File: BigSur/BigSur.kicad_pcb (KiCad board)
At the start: 2 copper layers, 123.5 x 131.5 mm, 152 parts, among them J1 XT30PW-M, J10 XT30PW-M, J12 XT30PW-M, J14 XT30PW-M, J15 XT30PW-M, J16 XT30PW-M, J2 XT30PW-M, J3 XT30PW-M, J4 XT30PW-M, J5 XT30PW-M, J6 XT30PW-M, J7 XT30PW-M, J8 XT30PW-M, J9 XT30PW-M, K1 G5LE-1A-VDDC12, K2 G5LE-1A-VDDC12, K3 G5LE-1A-VDDC12, K4 G5LE-1A-VDDC12, Q1 TSM900N10, Q2 TSM900N10, Q3 MMBT3904-7-F, Q4 MMBT3904-7-F, Q5 MMBT3904-7-F, Q6 MMBT3904-7-F, U1 DRV103H, U10 MCP6L02T-E_MS, U11 74LVC1G08W5-7, U12 ACS70331EESATR-2P5U3, U2 DRV103H, U3 DRV8806, U4 SMD46, U5 ACS70331EESATR-2P5U3, U6 ACS70331EESATR-2P5U3, U7 ACS70331EESATR-2P5U3, U8 ACS70331EESATR-2P5U3, U9 ACS70331EESATR-2P5U3

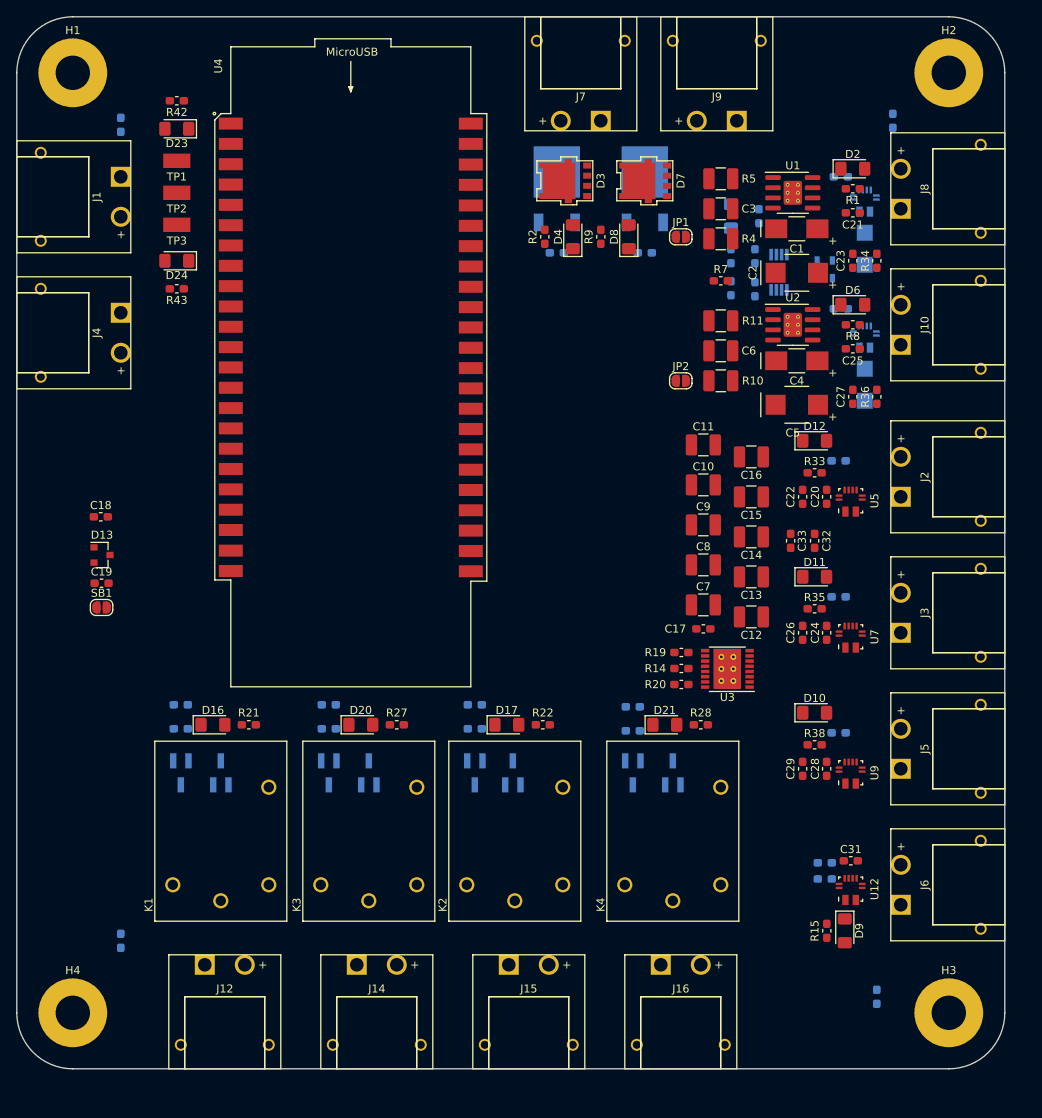
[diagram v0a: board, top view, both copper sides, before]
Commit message: Added custom 3d models for some parts, continued work on layout.
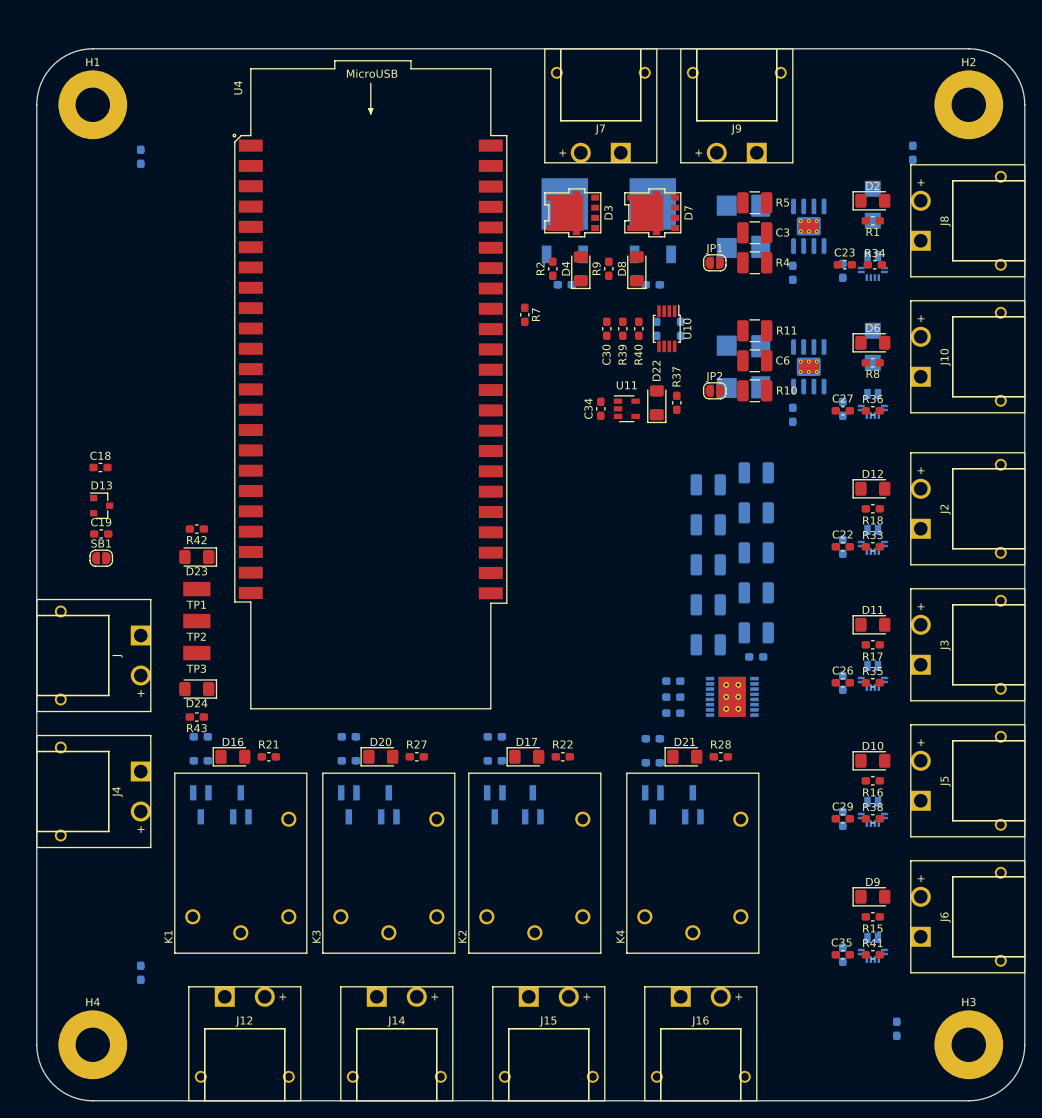
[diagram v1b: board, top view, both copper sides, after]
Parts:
- C1, C10, C11, C12, C13, C14, C15, C16, C17, C2, C20, C21, C24, C25, C28, C31, C32, C33, C4, C5, C7, C8, C9, R14, R19, R20, U1, U12, U2, U3, U5, U7, U9: moved to B.Cu
- C30, C34, C35, D22, R16, R17, R18, R37, R39, R40, R41, U10, U11: moved to F.Cu
- moved J 57.4 mm to (31.5, 100.3)
- moved J4 57.4 mm to (31.5, 117.3)
- moved D23 53.6 mm to (48.5, 88.0)
- moved D24 53.6 mm to (48.5, 104.5)
- moved R42 53.6 mm to (48.5, 84.5)
- moved R43 53.6 mm to (48.5, 108.0)
- moved TP1 53.6 mm to (48.5, 92.0)
- moved TP2 53.6 mm to (48.5, 96.0)
- moved TP3 53.6 mm to (48.5, 100.0)
- moved C32 31.3 mm to (109.0, 59.5), turned to 90 degrees
- moved C33 31.3 mm to (106.0, 59.5), turned to 90 degrees
- moved U11 30.3 mm to (102.2, 69.5), turned to 0 degrees
- moved R37 25.5 mm to (108.5, 68.8)
- moved D22 25.1 mm to (106.0, 68.8)
- moved C34 25.1 mm to (99.0, 69.5), turned to 270 degrees
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- renumbered J1 to J

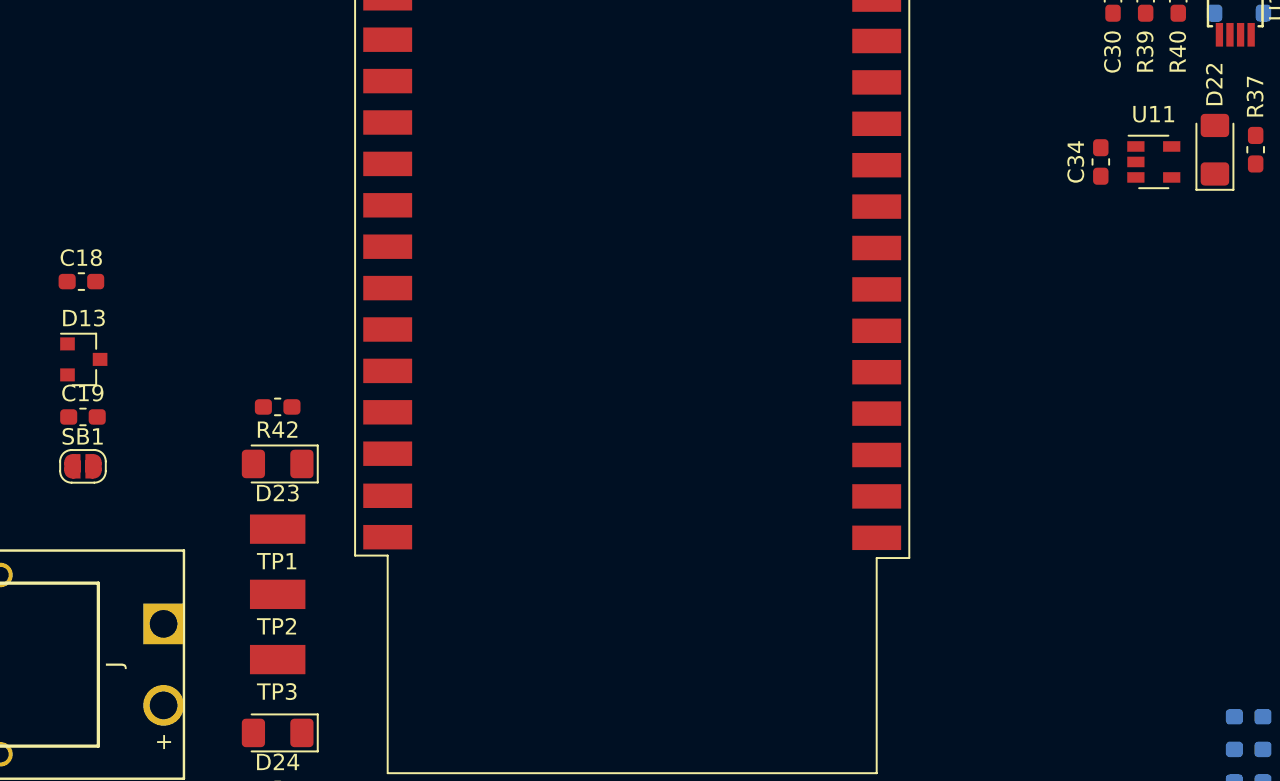
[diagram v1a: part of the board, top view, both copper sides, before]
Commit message: Made brake output active high in accordance with meeting decision
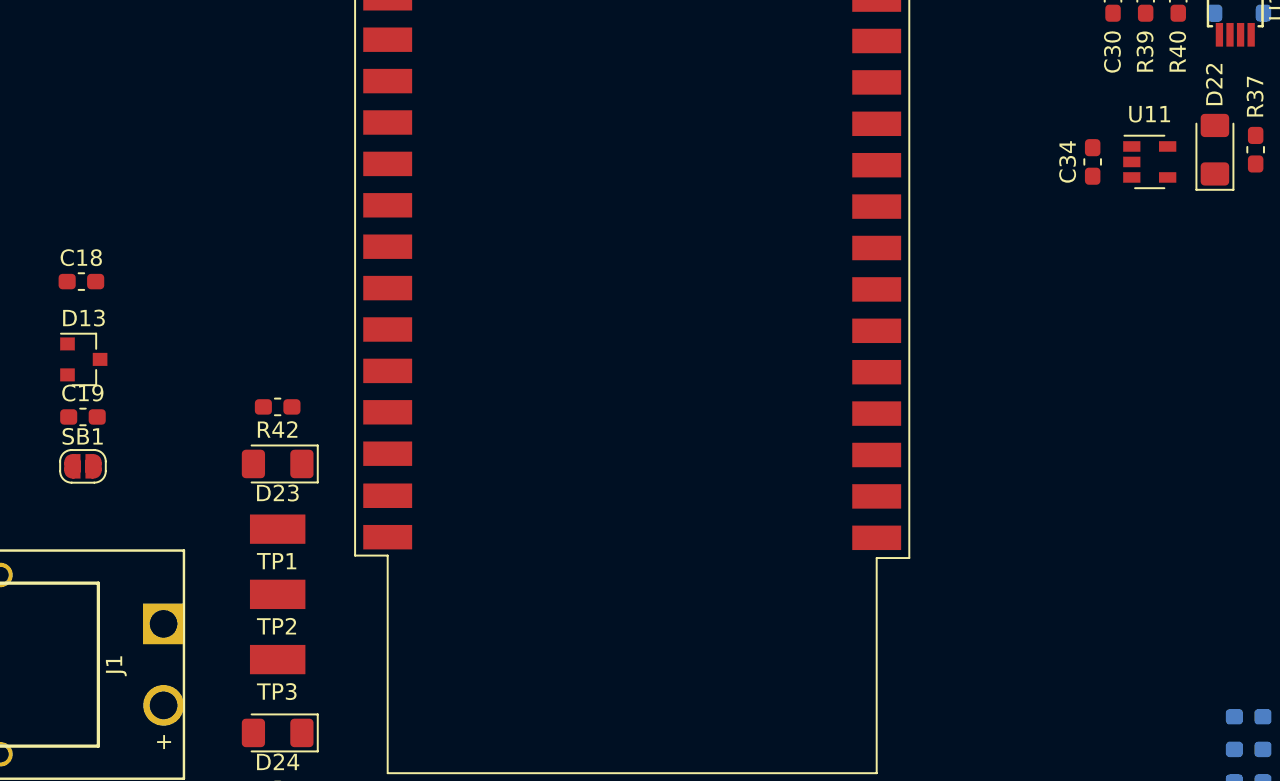
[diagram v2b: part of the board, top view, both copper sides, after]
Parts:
- U11: value 74LVC1G08W5-7 -> 74LVC1G00W5-7
- moved C34 0.50 mm to (98.5, 69.5)
- moved U11 0.25 mm to (102.0, 69.5)
- renumbered J to J1
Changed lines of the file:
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@@
-(kicad_pcb (version 20171130) (host pcbnew "(5.1.0)-1")
+(kicad_pcb (version 20171130) (host pcbnew "(5.1.4-0-10_14)")
   (general
     (thickness 1.6)
@@
   )
   (module Capacitor_SMD:C_0603_1608Metric_Pad1.05x0.95mm_HandSolder (layer F.Cu)
-    (at 99 69.5 270)
+    (at 98.5 69.5 270)
     (descr "Capacitor SMD 0603 (1608 Metric), square (rectangular) end terminal, IPC_7351 nominal with elongated pad for handsoldering. (Body size source: http://www.tortai-tech.com/upload/download/2011102023233369053.pdf), generated with kicad-footprint-generator")
     (tags "capacitor handsolder")
@@
   (module BigSur:AMASS_XT30PW-M (layer F.Cu)
     (at 31.5 100.34 90)
-    (fp_text reference J (at 0 7 90) (layer F.SilkS)
+    (fp_text reference J1 (at 0 7 90) (layer F.SilkS)
       (effects (font (size 1 1) (thickness 0.15)))
     )
@@
     )
   )
-  (module Package_TO_SOT_SMD:SOT-23-5 (layer F.Cu)
-    (at 102.25 69.5)
-    (descr "5-pin SOT23 package")
-    (tags SOT-23-5)
-    (attr smd)
-    (fp_text reference U11 (at 0 -2.9) (layer F.SilkS)
-      (effects (font (size 1 1) (thickness 0.15)))
-    )
-    (fp_text value 74LVC1G08W5-7 (at 0 2.9) (layer F.Fab)
-      (effects (font (size 1 1) (thickness 0.15)))
-    )
-    (fp_line (start 0.9 -1.55) (end 0.9 1.55) (layer F.Fab) (width 0.1))
-    (fp_line (start 0.9 1.55) (end -0.9 1.55) (layer F.Fab) (width 0.1))
-    (fp_line (start -0.9 -0.9) (end -0.9 1.55) (layer F.Fab) (width 0.1))
-    (fp_line (start 0.9 -1.55) (end -0.25 -1.55) (layer F.Fab) (width 0.1))
-    (fp_line (start -0.9 -0.9) (end -0.25 -1.55) (layer F.Fab) (width 0.1))
-    (fp_line (start -1.9 1.8) (end -1.9 -1.8) (layer F.CrtYd) (width 0.05))
-    (fp_line (start 1.9 1.8) (end -1.9 1.8) (layer F.CrtYd) (width 0.05))
-    (fp_line (start 1.9 -1.8) (end 1.9 1.8) (layer F.CrtYd) (width 0.05))
-    (fp_line (start -1.9 -1.8) (end 1.9 -1.8) (layer F.CrtYd) (width 0.05))
-    (fp_line (start 0.9 -1.61) (end -1.55 -1.61) (layer F.SilkS) (width 0.12))
-    (fp_line (start -0.9 1.61) (end 0.9 1.61) (layer F.SilkS) (width 0.12))
-    (fp_text user %R (at 0 0 -90) (layer F.Fab)
-      (effects (font (size 0.5 0.5) (thickness 0.075)))
-    )
-    (pad 5 smd rect (at 1.1 -0.95) (size 1.06 0.65) (layers F.Cu F.Paste F.Mask)
-      (net 7 +3V3))
-    (pad 4 smd rect (at 1.1 0.95) (size 1.06 0.65) (layers F.Cu F.Paste F.Mask)
-      (net 46 BRAKE_SOLENOID_LOW))
-    (pad 3 smd rect (at -1.1 0.95) (size 1.06 0.65) (layers F.Cu F.Paste F.Mask)
-      (net 1 GND))
-    (pad 2 smd rect (at -1.1 0) (size 1.06 0.65) (layers F.Cu F.Paste F.Mask)
-      (net 114 "Net-(U10-Pad7)"))
-    (pad 1 smd rect (at -1.1 -0.95) (size 1.06 0.65) (layers F.Cu F.Paste F.Mask)
-      (net 113 "Net-(U10-Pad1)"))
-    (model ${KISYS3DMOD}/Package_TO_SOT_SMD.3dshapes/SOT-23-5.wrl
-      (at (xyz 0 0 0))
-      (scale (xyz 1 1 1))
-      (rotate (xyz 0 0 0))
-    )
-  )
   (module BigSur:Allegro_QFN_ACS70331EESATR (layer B.Cu)
     (at 133 137 270)
@@
       (at (xyz 0 0 0))
       (scale (xyz 1 1 1))
+      (rotate (xyz 0 0 0))
+    )
+  )
+  (module Package_TO_SOT_SMD:SOT-23-5 (layer F.Cu)
+    (at 102 69.5)
+    (descr "5-pin SOT23 package")
+    (tags SOT-23-5)
+    (attr smd)
+    (fp_text reference U11 (at 0 -2.9) (layer F.SilkS)
+      (effects (font (size 1 1) (thickness 0.15)))
+    )
+    (fp_text value 74LVC1G00W5-7 (at 0 2.9) (layer F.Fab)
+      (effects (font (size 1 1) (thickness 0.15)))
+    )
+    (fp_text user %R (at 0 0 90) (layer F.Fab)
+      (effects (font (size 0.5 0.5) (thickness 0.075)))
+    )
+    (fp_line (start -0.9 1.61) (end 0.9 1.61) (layer F.SilkS) (width 0.12))
+    (fp_line (start 0.9 -1.61) (end -1.55 -1.61) (layer F.SilkS) (width 0.12))
+    (fp_line (start -1.9 -1.8) (end 1.9 -1.8) (layer F.CrtYd) (width 0.05))
+    (fp_line (start 1.9 -1.8) (end 1.9 1.8) (layer F.CrtYd) (width 0.05))
+    (fp_line (start 1.9 1.8) (end -1.9 1.8) (layer F.CrtYd) (width 0.05))
+    (fp_line (start -1.9 1.8) (end -1.9 -1.8) (layer F.CrtYd) (width 0.05))
+    (fp_line (start -0.9 -0.9) (end -0.25 -1.55) (layer F.Fab) (width 0.1))
+    (fp_line (start 0.9 -1.55) (end -0.25 -1.55) (layer F.Fab) (width 0.1))
+    (fp_line (start -0.9 -0.9) (end -0.9 1.55) (layer F.Fab) (width 0.1))
+    (fp_line (start 0.9 1.55) (end -0.9 1.55) (layer F.Fab) (width 0.1))
+    (fp_line (start 0.9 -1.55) (end 0.9 1.55) (layer F.Fab) (width 0.1))
+    (pad 1 smd rect (at -1.1 -0.95) (size 1.06 0.65) (layers F.Cu F.Paste F.Mask)
+      (net 113 "Net-(U10-Pad1)"))
+    (pad 2 smd rect (at -1.1 0) (size 1.06 0.65) (layers F.Cu F.Paste F.Mask)
+      (net 114 "Net-(U10-Pad7)"))
+    (pad 3 smd rect (at -1.1 0.95) (size 1.06 0.65) (layers F.Cu F.Paste F.Mask)
+      (net 1 GND))
+    (pad 4 smd rect (at 1.1 0.95) (size 1.06 0.65) (layers F.Cu F.Paste F.Mask)
+      (net 46 BRAKE_SOLENOID_LOW))
+    (pad 5 smd rect (at 1.1 -0.95) (size 1.06 0.65) (layers F.Cu F.Paste F.Mask)
+      (net 7 +3V3))
+    (model ${KISYS3DMOD}/Package_TO_SOT_SMD.3dshapes/SOT-23-5.wrl
+      (at (xyz 0 0 0))
+      (scale (xyz 1 1 1))

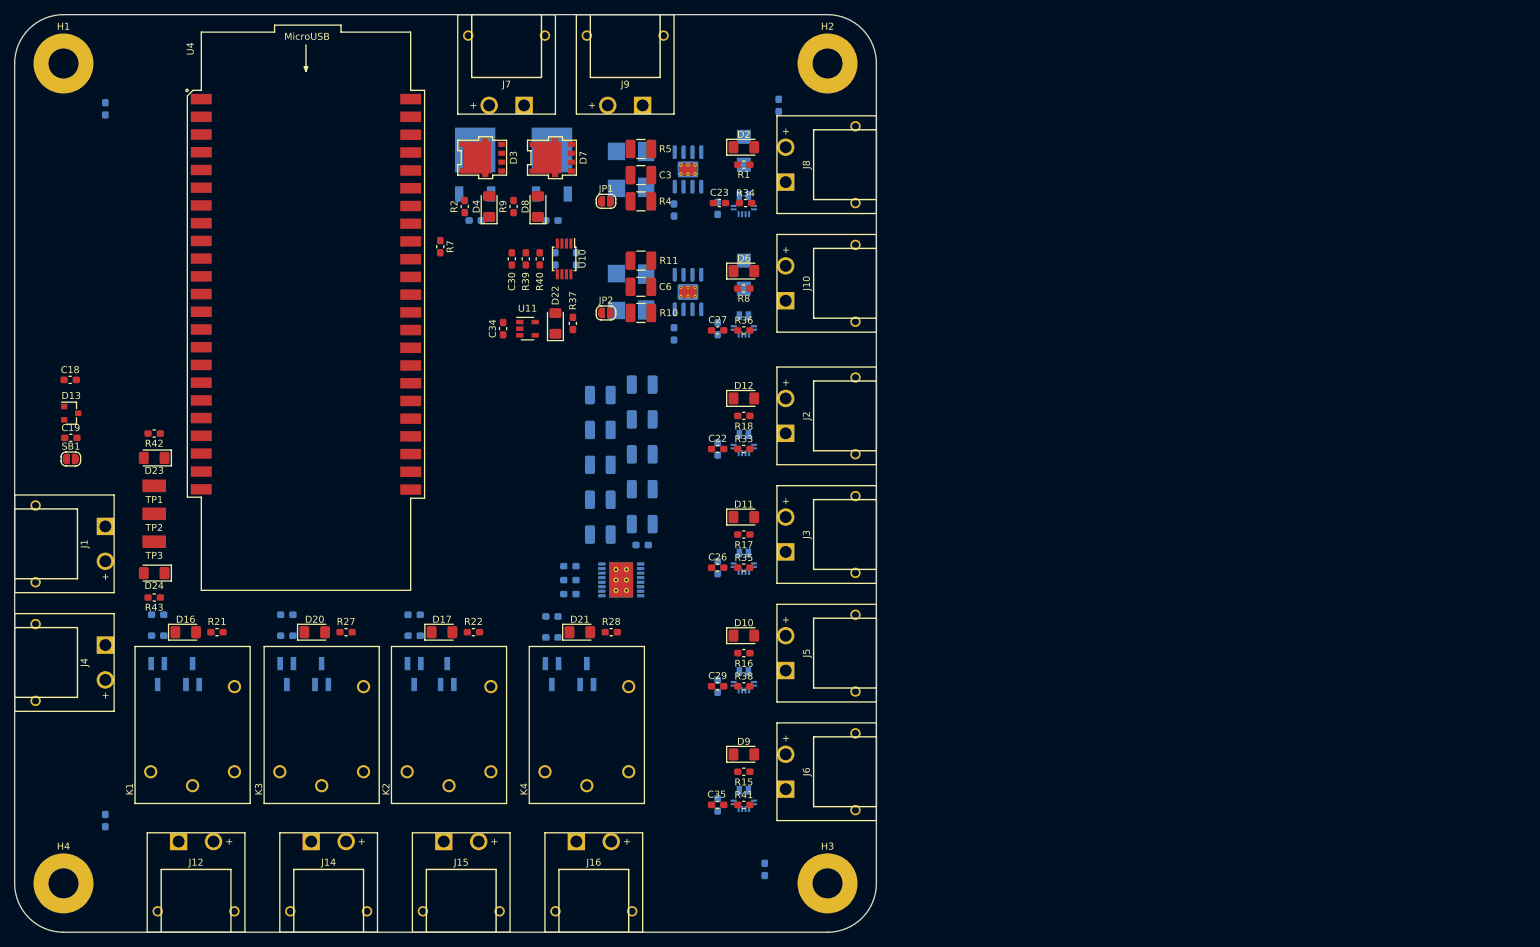
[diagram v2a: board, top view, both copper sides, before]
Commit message: Moved connectors to fit new LV plate layout
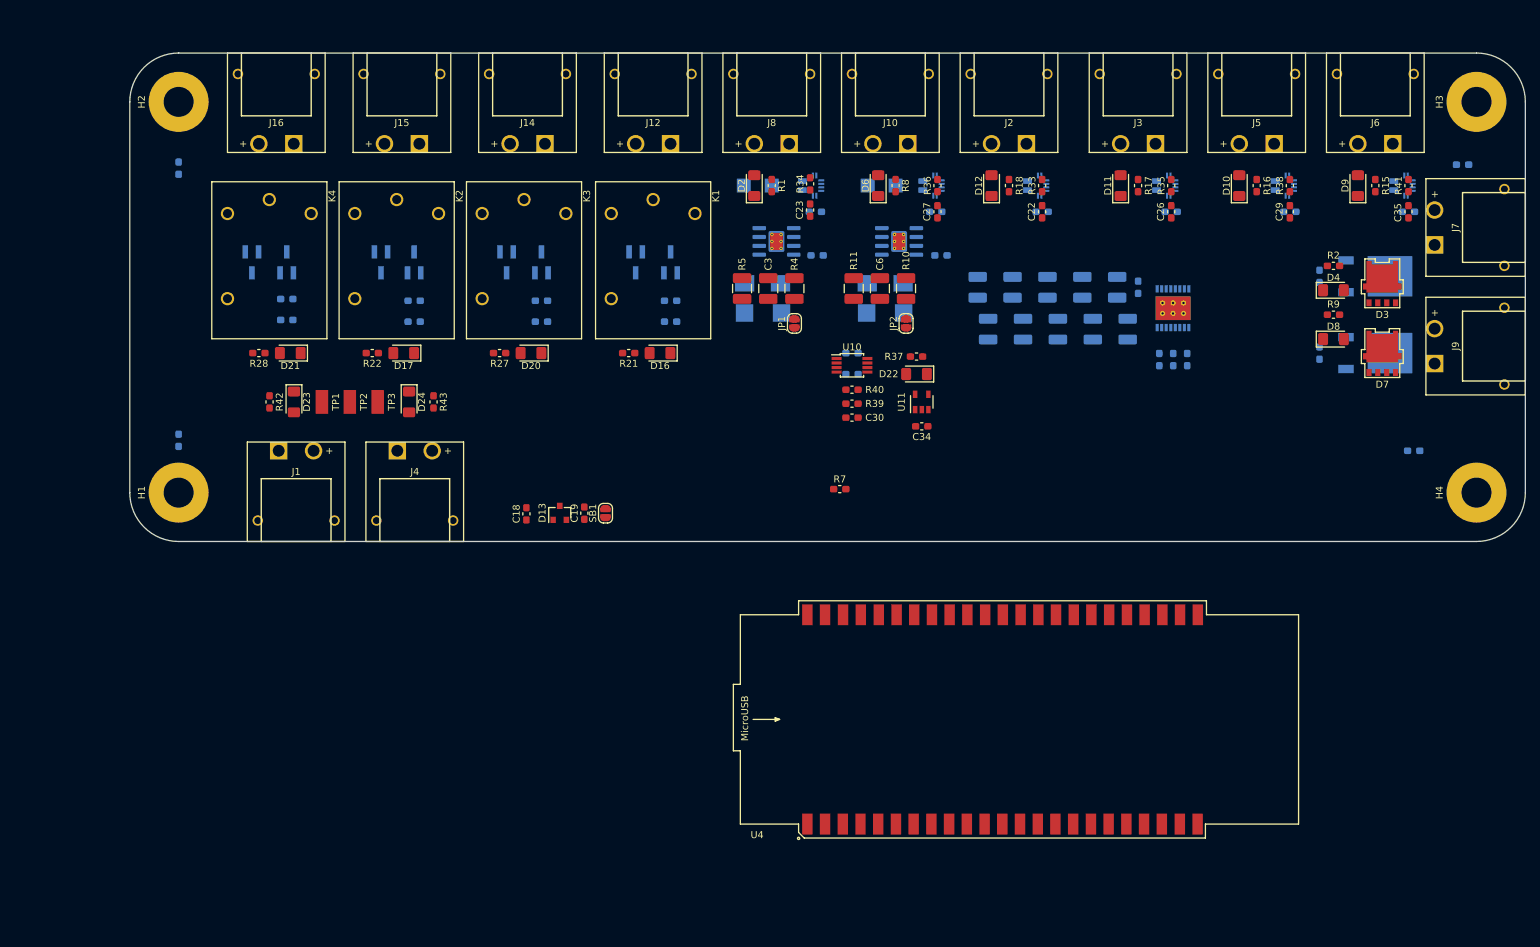
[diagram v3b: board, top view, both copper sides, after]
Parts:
- moved H4 210.1 mm to (238.0, 93.0), turned to 90 degrees
- moved C39 194.8 mm to (229.0, 87.0), turned to 180 degrees
- moved J7 145.6 mm to (242.0, 55.0), turned to 270 degrees
- moved H3 145.6 mm to (238.0, 37.0), turned to 90 degrees
- moved C38 142.1 mm to (236.0, 46.0), turned to 180 degrees
- moved J12 136.7 mm to (120.0, 33.0), turned to 0 degrees
- moved J9 133.6 mm to (242.0, 72.0), turned to 270 degrees
- moved C31 130.5 mm to (228.2, 52.8), turned to 0 degrees
- moved C35 130.5 mm to (228.2, 52.8), turned to 270 degrees
- moved D3 130.2 mm to (224.5, 63.0), turned to 180 degrees
- moved R41 130.2 mm to (228.2, 49.0), turned to 90 degrees
- moved Q1 130.0 mm to (223.5, 62.0), turned to 0 degrees
- moved U12 129.1 mm to (227.5, 49.0), turned to 0 degrees
- moved J16 128.3 mm to (66.0, 33.0), turned to 0 degrees
- moved R2 124.8 mm to (217.5, 60.5), turned to 0 degrees
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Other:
- board size 123.5 x 131.5 mm -> 200 x 70 mm
